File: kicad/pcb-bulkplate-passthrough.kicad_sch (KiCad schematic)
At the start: 1 part, among them J1 2601-3108

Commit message: done
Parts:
- removed J1: 2601-3108, 2601-3108:2601-3108, symbol Connector_Generic:Conn_01x08
- added H1: M3 Hole, MountingHole:MountingHole_3.2mm_M3, symbol Mechanical:MountingHole
- added J1: 2601-3104, 2601-3104:CONN4_2601-3104_WAG, symbol Connector_Generic:Conn_01x04
- added J2, J3: 2.54mm Header, Connector_PinSocket_2.54mm:PinSocket_1x02_P2.54mm_Vertical, symbol Connector_Generic:Conn_01x02
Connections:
- new net: J1.1 (Pin_1), J3.1 (Pin_1)
- new net: J1.2 (Pin_2), J3.2 (Pin_2)
- new net: J1.3 (Pin_3), J2.1 (Pin_1)
- new net: J1.4 (Pin_4), J2.2 (Pin_2)

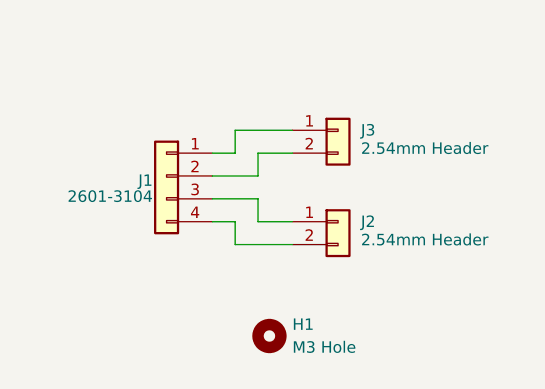
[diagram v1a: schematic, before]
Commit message: added 2 hole variant
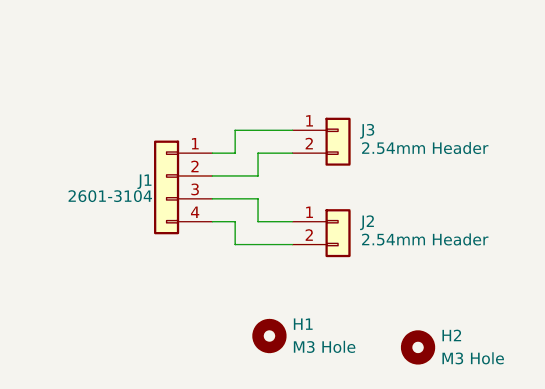
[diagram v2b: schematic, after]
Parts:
- added H2: M3 Hole, MountingHole:MountingHole_3.2mm_M3, symbol Mechanical:MountingHole
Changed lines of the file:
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@@
+	(symbol
+		(lib_id "Mechanical:MountingHole")
+		(at 153.67 110.49 0)
+		(unit 1)
+		(exclude_from_sim no)
+		(in_bom no)
+		(on_board yes)
+		(dnp no)
+		(fields_autoplaced yes)
+		(property "Reference" "H2"
+			(at 156.21 109.2199 0)
+			(effects
+				(font
+					(size 1.27 1.27)
+				)
+				(justify left)
+			)
+		)
+		(property "Value" "M3 Hole"
+			(at 156.21 111.7599 0)
+			(effects
+				(font
+					(size 1.27 1.27)
+				)
+				(justify left)
+			)
+		)
+		(property "Footprint" "MountingHole:MountingHole_3.2mm_M3"
+			(at 153.67 110.49 0)
+			(effects
+				(font
+					(size 1.27 1.27)
+				)
+				(hide yes)
+			)
+		)
+		(property "Datasheet" "~"
+			(at 153.67 110.49 0)
+			(effects
+				(font
+					(size 1.27 1.27)
+				)
+				(hide yes)
+			)
+		)
+		(property "Description" "Mounting Hole without connection"
+			(at 153.67 110.49 0)
+			(effects
+				(font
+					(size 1.27 1.27)
+				)
+				(hide yes)
+			)
+		)
+		(instances
+			(project "pcb-bulkplate-passthrough"
+				(path "/f83001a5-a57e-4459-b97b-0e5ff908a3b8"
+					(reference "H2")
+					(unit 1)
+				)
+			)
+		)
+	)
 	(symbol
 		(lib_id "Mechanical:MountingHole")
